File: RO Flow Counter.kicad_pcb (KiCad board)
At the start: 2 copper layers, 100 x 55 mm, 71 parts, among them J1 LCD Power, J2 Conn_01x12, J3 Barrel_Jack, J4 Conn_01x06, J5 Flow Meter, J6 Level Sensor (optional), J7 Conn_01x02, J8 Conn_01x04, K1 G5Q-1A, Q1 BC807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

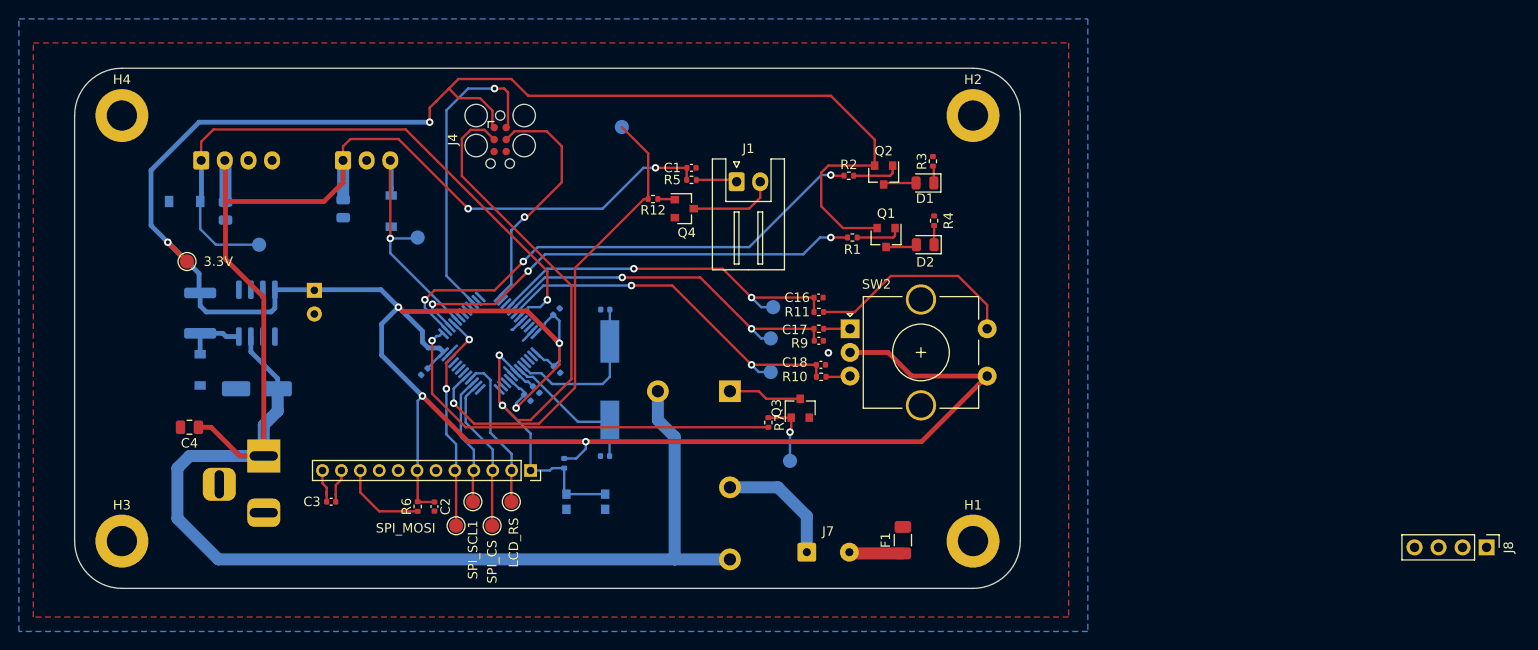
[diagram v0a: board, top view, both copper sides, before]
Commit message: change to esp32
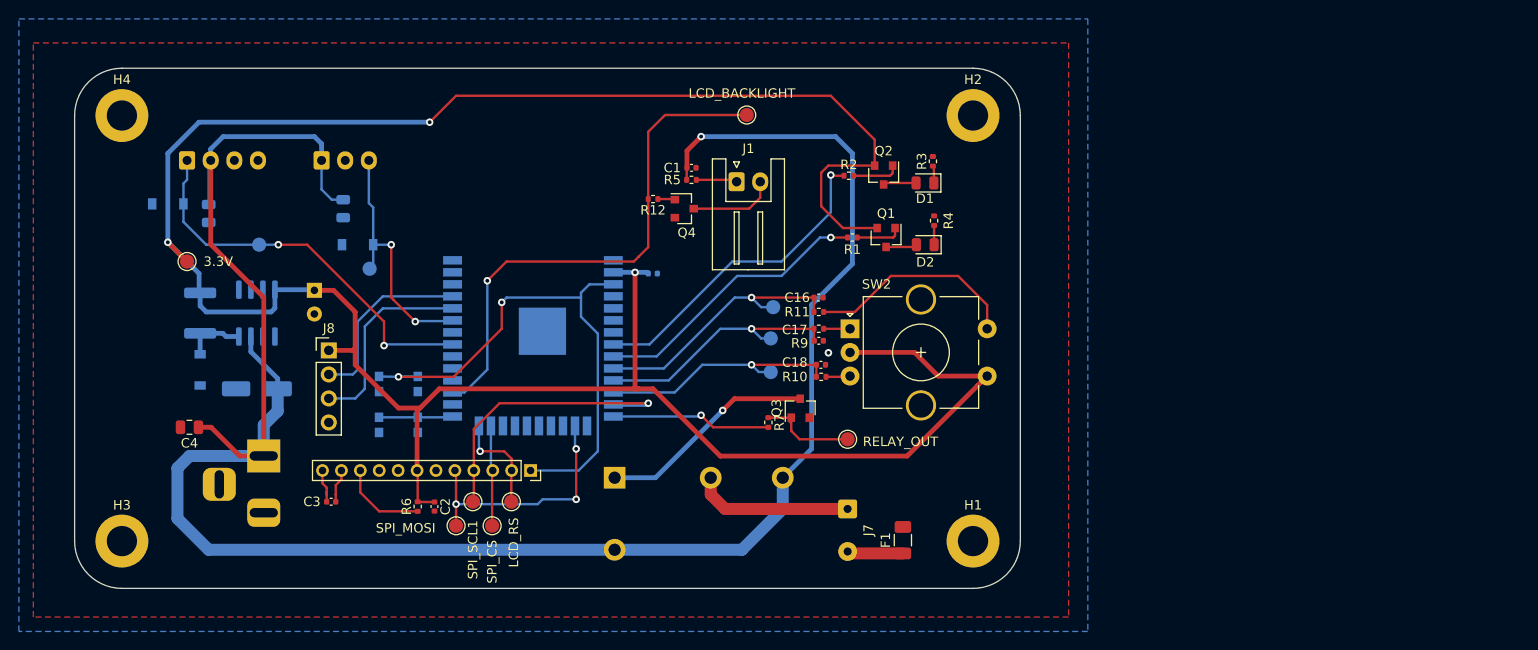
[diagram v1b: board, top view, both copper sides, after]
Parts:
- removed C10, C11, C7, C8, C9: 0.1uF, Capacitor_SMD:C_0402_1005Metric
- removed C12, C13: 15pF, Capacitor_SMD:C_0402_1005Metric
- removed J4: Conn_01x06, Connector:Tag-Connect_TC2030-IDC-FP_2x03_P1.27mm_Vertical
- removed R8: 10k, Resistor_SMD:R_0402_1005Metric
- removed SW1: Reset, Button_Switch_SMD:SW_Push_1P1T_NO_CK_KMR2
- removed Y1: 16MHz, Crystal:Crystal_SMD_HC49-SD
- added C19: 0.1uF, Capacitor_SMD:C_0402_1005Metric, B.Cu at (185.1, 76.7)
- added SW3: Reset, Button_Switch_SMD:SW_Push_1P1T_NO_CK_KMR2, B.Cu at (158.2, 88.4)
- added SW4: Flash Mode, Button_Switch_SMD:SW_Push_1P1T_NO_CK_KMR2, B.Cu at (158.2, 92.7)
- TP12, TP4: moved to F.Cu
- U2: value STM32F030C6Tx -> ESP32-WROOM-32; footprint Package_QFP:LQFP-48_7x7mm_P0.5mm -> RF_Module:ESP32-WROOM-32
- moved J8 124.2 mm to (150.9, 84.8), turned to 0 degrees
- moved K1 15.2 mm to (181.1, 98.3), turned to 0 degrees
- moved TP12 13.3 mm to (195.1, 59.9)
- moved TP4 6.51 mm to (205.7, 94.2)
- moved J7 6.29 mm to (205.7, 101.6), turned to 270 degrees
- moved TP9 6.06 mm to (155.2, 76.2), turned to 180 degrees
- moved D4 5.03 mm to (153.9, 73.7), turned to 180 degrees
- moved U2 4.60 mm to (172.5, 83.6), turned to 180 degrees
- moved J5 2.27 mm to (150.1, 64.7)
- moved C15 1.80 mm to (138.2, 70.4)
- moved D5 1.80 mm to (133.9, 69.3)
- moved J6 1.49 mm to (135.9, 64.7)
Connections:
- D4 pad 1: /sensors/FLOW_OUT -> /mcu/FLOW_IN
- J5 pad 3: /sensors/FLOW_OUT -> /mcu/FLOW_IN
- J8 pad 2: (no net) -> /mcu/TX
- J8 pad 3: (no net) -> /mcu/RX
- TP9 pad 1: /sensors/FLOW_OUT -> /mcu/FLOW_IN
- U2 pad 1: +3V3 -> GND
- U2 pad 11: (no net) -> /mcu/RE_A
- U2 pad 12: (no net) -> /mcu/RE_B
- U2 pad 13: (no net) -> /display/SCL
- U2 pad 14: /display/CS -> /mcu/RELAY_OUT
- U2 pad 15: /display/SCL -> GND
- U2 pad 16: /mcu/LCD_RS -> /display/MOSI
- U2 pad 17: /display/BACKLIGHT_LCD -> (no net)
- U2 pad 2: (no net) -> +3V3
- U2 pad 23: GND -> /display/CS
- U2 pad 24: +3V3 -> /mcu/LCD_RS
- U2 pad 25: /mcu/RELAY_OUT -> Net-(R14-Pad2)
- U2 pad 26: /mcu/ERROR_OUT -> (no net)
- U2 pad 27: /mcu/NORMAL_OPERATION_OUT -> /display/BACKLIGHT_LCD
- U2 pad 28: /display/MOSI -> (no net)
- U2 pad 29: /sensors/FLOW_OUT -> (no net)
- U2 pad 3: (no net) -> /display/NRST
- U2 pad 31: (no net) -> /mcu/LEVEL_IN
- U2 pad 33: (no net) -> /mcu/FLOW_IN
- U2 pad 34: /mcu/SWD_IO -> /mcu/RX
- U2 pad 35: (no net) -> /mcu/TX
- U2 pad 37: /mcu/SWD_CLK -> (no net)
- U2 pad 38: (no net) -> GND
- U2 pad 39: (no net) -> GND
- U2 pad 5: Net-(C12-Pad1) -> (no net)
- U2 pad 6: Net-(C13-Pad1) -> (no net)
- U2 pad 7: /display/NRST -> (no net)
- U2 pad 8: GND -> /mcu/ERROR_OUT
- U2 pad 9: +3V3 -> /mcu/NORMAL_OPERATION_OUT
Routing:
- net +3V3: track 315.5 -> 267.1 mm, vias 7 -> 3
- net /mcu/SWD_IO: track 33.8 -> 0.00 mm, vias 1 -> 0
- net /mcu/FLOW_IN: track 0.00 -> 27.1 mm, vias 0 -> 2
- net /mcu/RELAY_OUT: track 44.2 -> 17.2 mm
- net /sensors/FLOW_OUT: track 26.6 -> 0.00 mm, vias 1 -> 0
- net /mcu/SWD_CLK: track 25.7 -> 0.00 mm, vias 1 -> 0
- net /mcu/LEVEL_IN: track 66.0 -> 42.6 mm, vias 1 -> 2
- net /mcu/RX: track 0.00 -> 20.9 mm
- net /mcu/ERROR_OUT: track 54.3 -> 34.1 mm, vias 3 -> 1
- net /mcu/NORMAL_OPERATION_OUT: track 49.9 -> 30.0 mm, vias 3 -> 1
- net /mcu/TX: track 0.00 -> 19.5 mm
- net /display/SCL: track 13.8 -> 31.3 mm, vias 0 -> 1
- net Net-(C12-Pad1): track 17.5 -> 0.00 mm
- net /display/NRST: track 73.3 -> 57.8 mm
- net Net-(C13-Pad1): track 15.5 -> 0.00 mm
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
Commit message: v1
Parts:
- removed C15: 4.7uF, Capacitor_SMD:C_0805_2012Metric
- removed TP10: LEVEL_OUT, TestPoint:TestPoint_Pad_D1.5mm
- added G***: LOGO, Custom Footprints:puppy_symbol, B.Cu at (198.6, 62.2)
- added R13: 10k, Resistor_SMD:R_0402_1005Metric, B.Cu at (155.7, 88.1)
- added R14: 10k, Resistor_SMD:R_0402_1005Metric, B.Cu at (155.7, 91.5)
- added R15: 10k, Resistor_SMD:R_0402_1005Metric, B.Cu at (156.5, 68.3)
- added R16: 1k, Resistor_SMD:R_0402_1005Metric, B.Cu at (162.8, 85.3)
- added R17: 1k, Resistor_SMD:R_0402_1005Metric, B.Cu at (162.8, 84.1)
- added R18: 1k56, Resistor_SMD:R_0402_1005Metric, B.Cu at (137.4, 69.6)
- added R19: 1k56, Resistor_SMD:R_0402_1005Metric, B.Cu at (156.5, 69.8)
- added R20: 1k, Resistor_SMD:R_0402_1005Metric, B.Cu at (174.8, 101.3)
- added R8: 10k, Resistor_SMD:R_0402_1005Metric, B.Cu at (137.4, 68.3)
- C1, C17, C18, J8, Q3, Q4, R10, R11, R12, R5, R7, R9, TP1, TP12: moved to B.Cu
- C16: value 0.1uF -> 100nF; moved to B.Cu
- J1: footprint Connector_JST:JST_XH_S2B-XH-A_1x02_P2.50mm_Horizontal -> Connector_PinHeader_2.54mm:PinHeader_1x02_P2.54mm_Vertical
- J5: footprint Connector_JST:JST_XH_S3B-XH-A_1x03_P2.50mm_Horizontal -> Connector_JST:JST_XH_S3B-XH-A-1_1x03_P2.50mm_Horizontal
- J6: footprint Connector_JST:JST_XH_S4B-XH-A_1x04_P2.50mm_Horizontal -> Connector_JST:JST_XH_S4B-XH-A-1_1x04_P2.50mm_Horizontal
- J7: footprint Connector_Wire:SolderWire-0.25sqmm_1x02_P4.5mm_D0.65mm_OD2mm -> Connector_Wire:SolderWire-0.75sqmm_1x02_P7mm_D1.25mm_OD3.5mm
- TP11: value SPI_SCL1 -> SCL
- TP6: value SPI_CS -> SDA
- TP7: value SPI_MOSI -> LEVEL_IN; moved to B.Cu
- TP8: value LCD_RS -> RESET_LCD
- TP9: value FLOW_OUT -> FLOW_IN
- moved TP7 39.9 mm to (139.4, 72.1), turned to 180 degrees
- moved TP12 34.8 mm to (194.3, 94.7)
- moved TP4 31.7 mm to (176.3, 105.9), turned to 180 degrees
- moved R12 28.2 mm to (199.4, 93.2)
- moved Q3 25.7 mm to (177.0, 100.8), turned to 0 degrees
- moved Q4 23.3 mm to (198.9, 90.7), turned to 90 degrees
- moved R7 19.9 mm to (178.1, 97.3), turned to 90 degrees
- moved C1 16.1 mm to (197.6, 79.2), turned to 90 degrees
- moved J1 15.8 mm to (198.9, 82.0)
- moved R5 15.8 mm to (198.9, 79.2), turned to 90 degrees
- moved D5 7.37 mm to (141.2, 69.1), turned to 0 degrees
- moved TP2 4.88 mm to (194.1, 77.2), turned to 180 degrees
- moved D4 4.86 mm to (152.8, 68.9)
- moved TP9 4.13 mm to (154.4, 72.1)
- moved TP6 4.07 mm to (164.1, 103.6)
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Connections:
- D4 pad 1: /mcu/FLOW_IN -> Net-(D4-Pad1)
- D5 pad 1: /mcu/LEVEL_IN -> Net-(D5-Pad1)
- J2 pad 1: /display/NRST -> /display/RESET_DISPLAY
- J2 pad 10: Net-(J2-Pad10) -> GND
- J2 pad 2: /mcu/LCD_RS -> (no net)
- J2 pad 3: /display/CS -> (no net)
- J2 pad 5: /display/MOSI -> /display/SDA
- J2 pad 9: GND -> Net-(J2-Pad9)
- J5 pad 3: /mcu/FLOW_IN -> Net-(J5-Pad3)
- J6 pad 1: /mcu/LEVEL_IN -> Net-(J6-Pad1)
- R6 pad 1: Net-(J2-Pad10) -> Net-(J2-Pad9)
- SW3 pad 2: /display/NRST -> Net-(R13-Pad2)
- TP6 pad 1: /display/CS -> /display/SDA
- TP7 pad 1: /display/MOSI -> Net-(D5-Pad1)
- TP8 pad 1: /mcu/LCD_RS -> /display/RESET_DISPLAY
- TP9 pad 1: /mcu/FLOW_IN -> Net-(D4-Pad1)
- U2 pad 13: /display/SCL -> (no net)
- U2 pad 16: /display/MOSI -> (no net)
- U2 pad 23: /display/CS -> (no net)
- U2 pad 24: /mcu/LCD_RS -> /display/RESET_DISPLAY
- U2 pad 3: /display/NRST -> Net-(R13-Pad2)
- U2 pad 30: (no net) -> /mcu/LEVEL_IN
- U2 pad 31: /mcu/LEVEL_IN -> /mcu/FLOW_IN
- U2 pad 33: /mcu/FLOW_IN -> /display/SDA
- U2 pad 36: (no net) -> /display/SCL
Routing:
- net /display/NRST: track 57.8 -> 0.00 mm, vias 2 -> 0
- net +24V: track 227.0 -> 172.1 mm, vias 1 -> 2
- net /mcu/LEVEL_IN: track 42.6 -> 2.47 mm, vias 2 -> 0
- net Net-(R13-Pad2): track 0.00 -> 36.5 mm, vias 0 -> 2
- net Net-(D5-Pad1): track 0.00 -> 35.7 mm, vias 0 -> 3
- net /display/MOSI: track 26.6 -> 0.00 mm, vias 3 -> 0
- net /display/SDA: track 0.00 -> 25.7 mm, vias 0 -> 1
- net /mcu/FLOW_IN: track 27.1 -> 2.47 mm, vias 2 -> 0
- net Net-(D4-Pad1): track 0.00 -> 22.8 mm, vias 0 -> 2
- net Net-(K1-Pad1): track 23.1 -> 5.16 mm, vias 1 -> 0
- net /display/BACKLIGHT_LCD: track 55.9 -> 43.0 mm, vias 1 -> 2
- net /display/RESET_DISPLAY: track 0.00 -> 11.0 mm
- net /mcu/LCD_RS: track 11.0 -> 0.00 mm, vias 1 -> 0
- net /display/CS: track 10.7 -> 0.00 mm
- net Net-(J2-Pad10): track 9.21 -> 0.00 mm
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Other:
- board text added: "+24V DC"
- board text added: "Error"
- board text added: "Normal"
- board text added: "RO Flow counter v0.1"
- board text added: "Rx"
- board text added: "Tx"

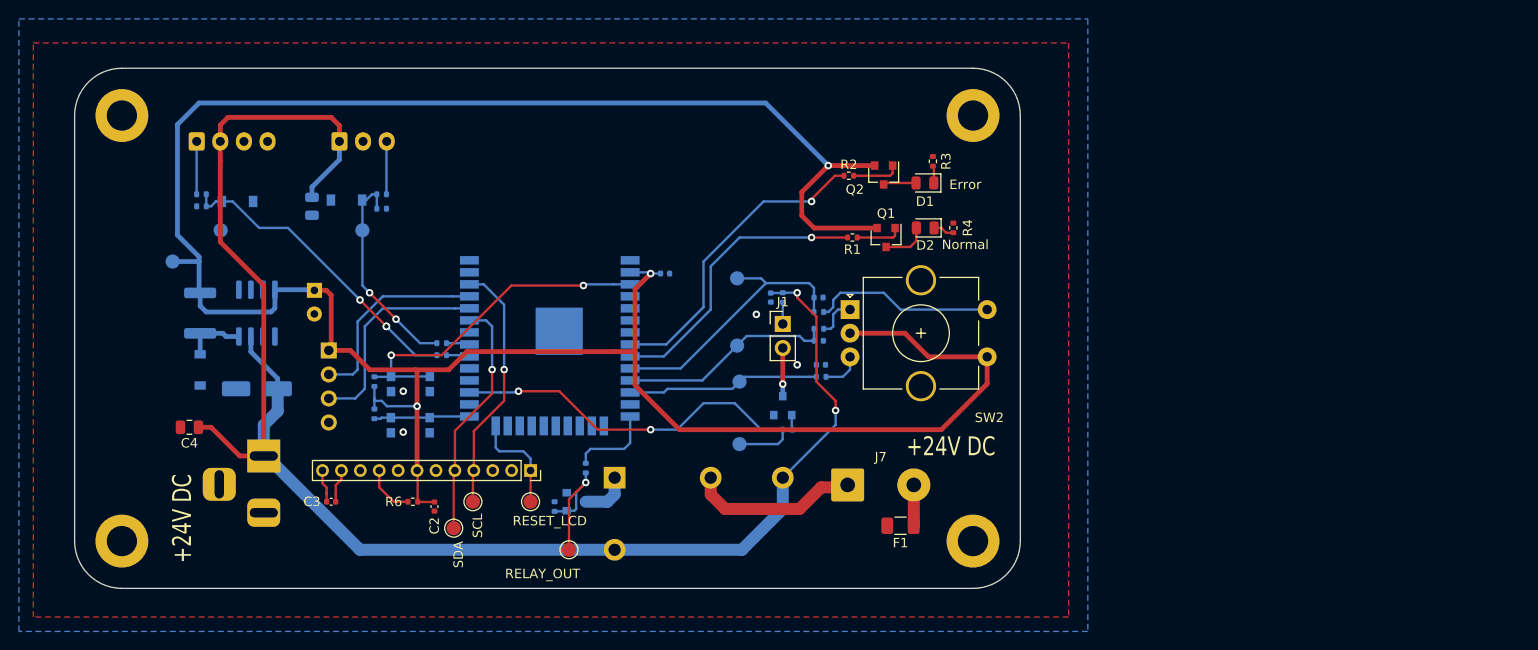
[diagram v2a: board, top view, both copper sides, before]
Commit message: fix rotary encoder, i2c pullup resistors, reset button placement
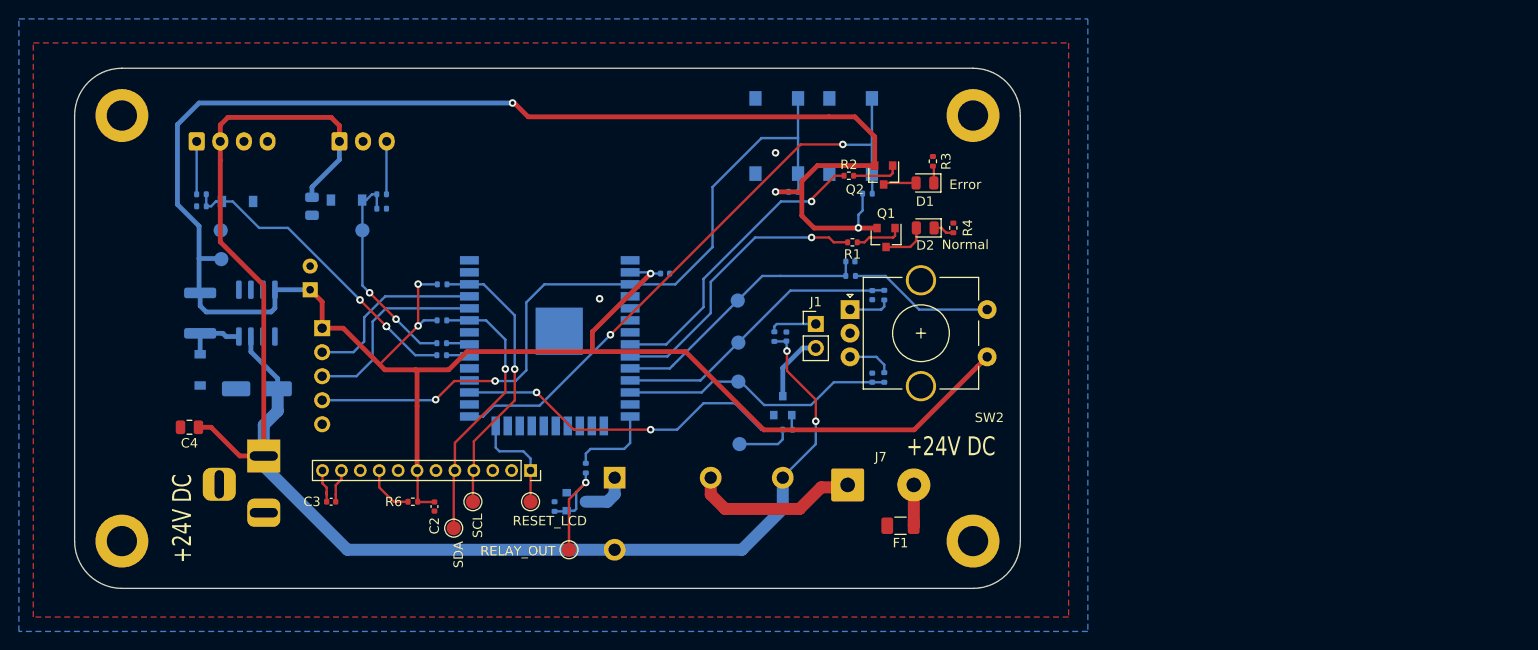
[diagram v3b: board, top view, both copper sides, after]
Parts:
- removed G***: LOGO, Custom Footprints:puppy_symbol
- added R21: 5k6, Resistor_SMD:R_0402_1005Metric, B.Cu at (162.8, 81.7)
- added R22: 5k6, Resistor_SMD:R_0402_1005Metric, B.Cu at (162.9, 77.9)
- J8: value Conn_01x04 -> Programming; footprint Connector_PinHeader_2.54mm:PinHeader_1x04_P2.54mm_Vertical -> Connector_PinHeader_2.54mm:PinHeader_1x05_P2.54mm_Vertical
- R1, R2: value 1M -> 10k
- R15: value 10k -> 42.2k
- R19: value 1k56 -> 5k6
- R20: value 1k -> 10k
- SW3, SW4: footprint Button_Switch_SMD:SW_Push_1P1T_NO_CK_KMR2 -> Button_Switch_SMD:SW_Push_1P1T_NO_6x6mm_H9.5mm
- moved R14 57.1 mm to (207.8, 68.3), turned to 0 degrees
- moved SW4 55.7 mm to (206.1, 62.2), turned to 90 degrees
- moved R13 48.7 mm to (200.0, 68.1), turned to 0 degrees
- moved SW3 46.8 mm to (198.2, 62.2), turned to 270 degrees
- moved R9 7.78 mm to (209.6, 79.0), turned to 90 degrees
- moved C17 7.43 mm to (208.3, 79.0), turned to 270 degrees
- moved R10 6.67 mm to (209.6, 87.7), turned to 270 degrees
- moved C18 5.59 mm to (208.3, 87.7), turned to 90 degrees
- moved TP1 5.15 mm to (139.5, 75.2)
- moved C16 5.08 mm to (206.0, 75.4)
- moved R11 5.08 mm to (206.1, 77.0)
- moved C1 4.45 mm to (199.3, 83.4), turned to 270 degrees
- moved R5 4.22 mm to (198.0, 83.4), turned to 270 degrees
- moved J1 3.49 mm to (202.4, 82.0)
- moved J8 2.45 mm to (150.2, 82.5)
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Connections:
- J8 pad 4: GND -> /mcu/reset
- R13 pad 2: Net-(R13-Pad2) -> /mcu/reset
- SW2 pad C: +3V3 -> GND
- SW3 pad 2: Net-(R13-Pad2) -> /mcu/reset
- U2 pad 3: Net-(R13-Pad2) -> /mcu/reset
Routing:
- net /mcu/reset: track 0.00 -> 79.6 mm, vias 0 -> 2
- net Net-(R14-Pad2): track 10.1 -> 64.6 mm, vias 0 -> 2
- net Net-(R13-Pad2): track 36.5 -> 0.00 mm, vias 2 -> 0
- net /mcu/RE_A: track 22.9 -> 30.8 mm
- net /mcu/RE_B: track 21.6 -> 29.4 mm
- net +24V: track 172.1 -> 164.9 mm
- net +3V3: track 270.1 -> 274.3 mm, vias 3 -> 6
- net Net-(R11-Pad2): track 19.3 -> 15.4 mm
- net /display/SDA: track 25.7 -> 29.2 mm
- net /display/SCL: track 26.8 -> 30.1 mm
- net Net-(J1-Pad2): track 5.10 -> 7.81 mm, vias 1 -> 0
- net Net-(J1-Pad1): track 2.79 -> 5.06 mm
- net /mcu/TX: track 21.3 -> 19.5 mm
- net /mcu/RX: track 22.7 -> 20.9 mm
- net /mcu/ERROR_OUT: track 33.2 -> 32.1 mm
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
